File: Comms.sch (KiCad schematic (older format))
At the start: 50 parts, among them J1 arm connector, J2 USB_B_Micro, J6 logic-side RS485 debug/expans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, J8 power-side RS485 debug/expans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, U1 93LCxxB, U2 FT232H, U3 ADM2682E, U4 TPD2E2U06DCK, U5 TPD2E2U06DCK, Y1 12MHz

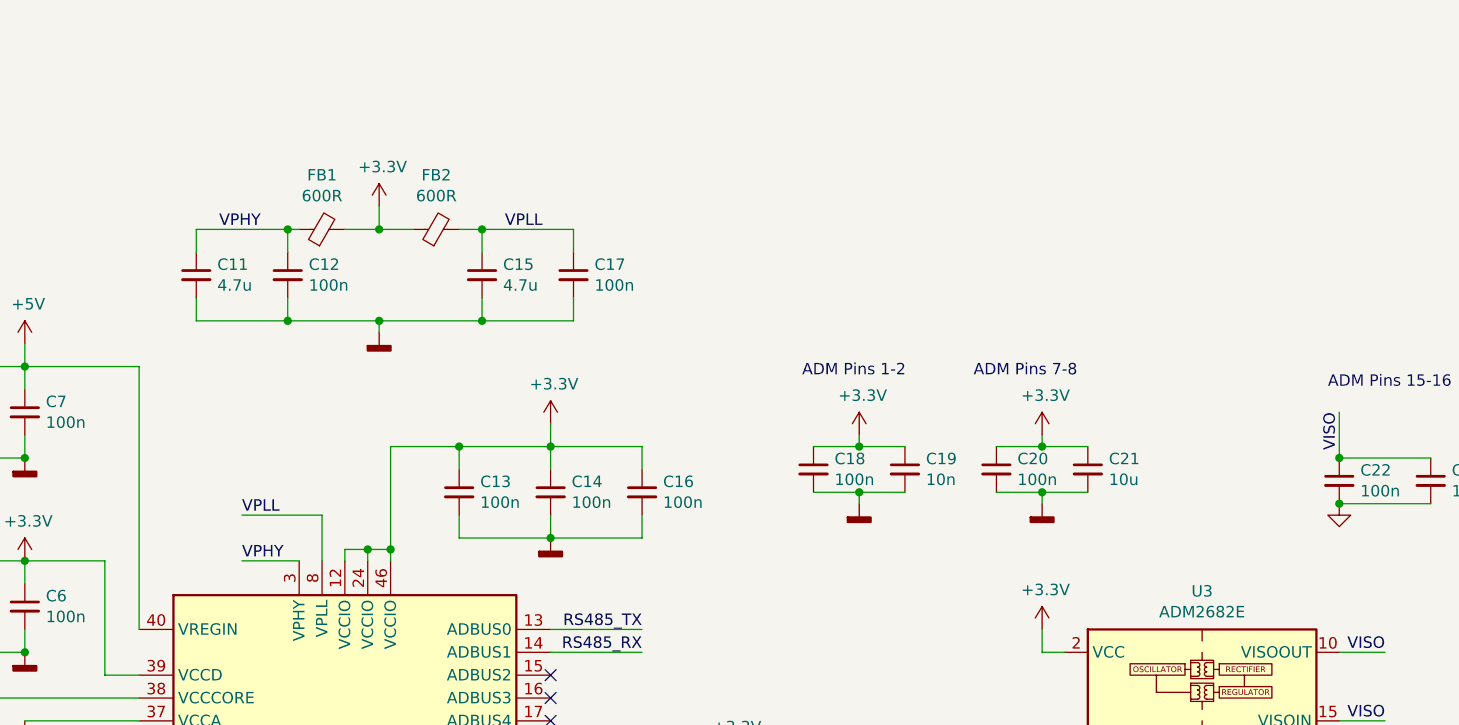
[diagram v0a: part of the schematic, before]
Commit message: working through the power subsystems now. changed e-stop topology.
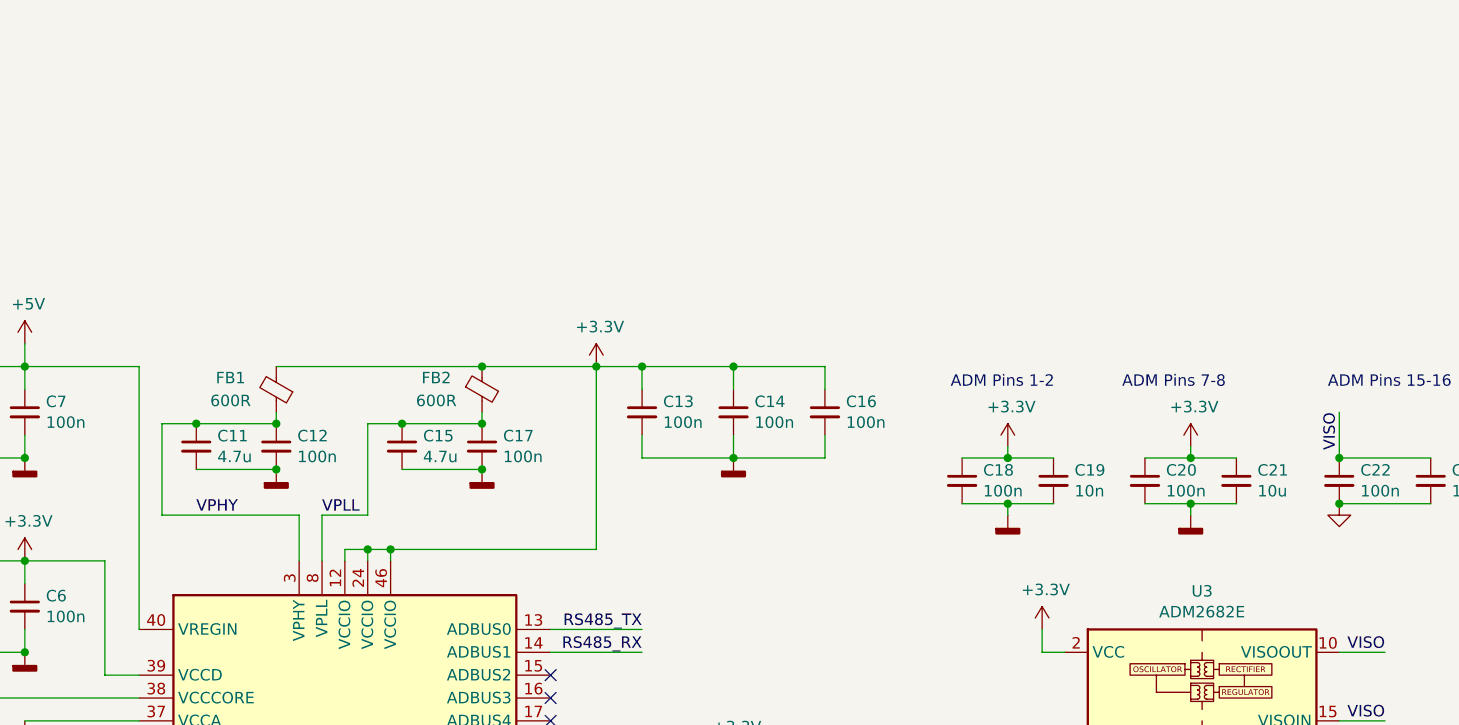
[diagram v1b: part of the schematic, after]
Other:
- moved on the sheet: C11, C12, C13, C14, C15, C16, C17, C18, C19, C20, C21, FB1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

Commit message: ready to generate CAM
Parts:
- added C49: 22u, Capacitor_SMD:C_1206_3216Metric, symbol Device:C_Small
- added C50: 4n7, Capacitor_SMD:C_0603_1608Metric, symbol Device:C_Small
- added C51: 47u, Capacitor_SMD:C_1206_3216Metric, symbol Device:C_Small
- added R20: 437k, Resistor_SMD:R_0603_1608Metric, symbol Device:R_Small
- added R22: 140k, Resistor_SMD:R_0603_1608Metric, symbol Device:R_Small
- added U11: LMZ21700SIL, BLDC:SIL0008E, symbol BLDC:LMZ21700SILT
- C1, C12, C13, C14, C16, C17, C18, C20, C22, C24, C4, C6, C7, C8: D1PN 1276-1258-1-ND -> 311-1344-1-ND; MFN Samsung -> Yageo; MPN CL10F104ZO8NNNC -> CC0603KRX7R9BB104
- C11, C15, C2, C3: Maximum Voltage (none) -> 10 V; Tolerance (none) -> 10%
- D1: value LED -> GREEN
- D2: value LED -> RED; D1PN 732-4980-1-ND -> 732-4978-1-ND; MPN 150060VS75000 -> 150060RS75000
- J1: D1PN 0436500511-ND -> WM1888CT-ND; MPN 436500511 -> 436500510
- R23: D1N (none) -> Digikey; D1PN (none) -> 311-120HRCT-ND; MFN (none) -> Yageo; MPN (none) -> RC0603FR-07120RL; Tolerance (none) -> 1%
- R3: value 2k -> 2.2k; D1PN P2.0KDBCT-ND -> 311-2.20KHRCT-ND; MFN Panasonic -> Yageo; MPN ERA-3AEB202V -> RC0603FR-072K2L; Tolerance (none) -> 1%
- R6: Tolerance (none) -> 0.1%
- R7, R8: D1PN A130089CT-ND -> 311-470HRCT-ND; MFN TE Connectivity -> Yageo; MPN CRGCQ0603J470R -> RC0603FR-07470RL; Tolerance (none) -> 1%
- U3: D1PN ADM2682EBRIZ-RL7CT-ND -> ADM2682EBRIZ-ND; MPN ADM2682EBRIZ-RL7 -> ADM2682EBRIZ
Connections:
- net +3V3: now also C51.1, R20.1, U11.4 (VOUT), U11.6 (VOS); no longer C1.1, C13.1, C14.1, C16.1, C2.1, C6.1, D1.2 (A), D2.2 (A), FB1.2, FB2.1, R1.1, R2.1, R4.1, R5.2, U1.8 (VCC), U2.12 (VCCIO), U2.24 (VCCIO), U2.39 (VCCD), U2.46 (VCCIO)
- net +5V: now also C49.2, U11.7 (EN), U11.8 (VIN)
- net GNDD: now also C49.1, C50.1, C51.2, R22.2, U11.5 (GND), U11.9 (PAD)
- net RXLED: now reaches R7.2, U2.27 (ACBUS3)
- net TXLED: now reaches R8.2, U2.28 (ACBUS4)
- new net: R20.2, R22.1, U11.2 (FB)
- new net: C50.2, U11.1 (SS)
- new net FT232H_3V3: C1.1, C13.1, C14.1, C16.1, C2.1, C6.1, D1.2 (A), D2.2 (A), FB1.2, FB2.1, R1.1, R2.1, R4.1, R5.2, U1.8 (VCC), U2.12 (VCCIO), U2.24 (VCCIO), U2.39 (VCCD), U2.46 (VCCIO)
- no-connect marks 13 -> 14
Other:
- note added: "soft-start ramp time = 2.3ms"
